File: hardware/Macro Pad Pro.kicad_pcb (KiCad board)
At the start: 2 copper layers, 107 x 134 mm, 149 parts, among them J1 USB_C, J2 Conn_02x08_Odd_Even, J4 Conn_02x01, SW1 SW_Push_B, SW2 SW_Push_R, U1 RP2040, U2 OLED, U3 AP2112K-3.3, U4 USBLC6-2SC6, U6 W25Q128JVS, Y1 ABM8-272-T3

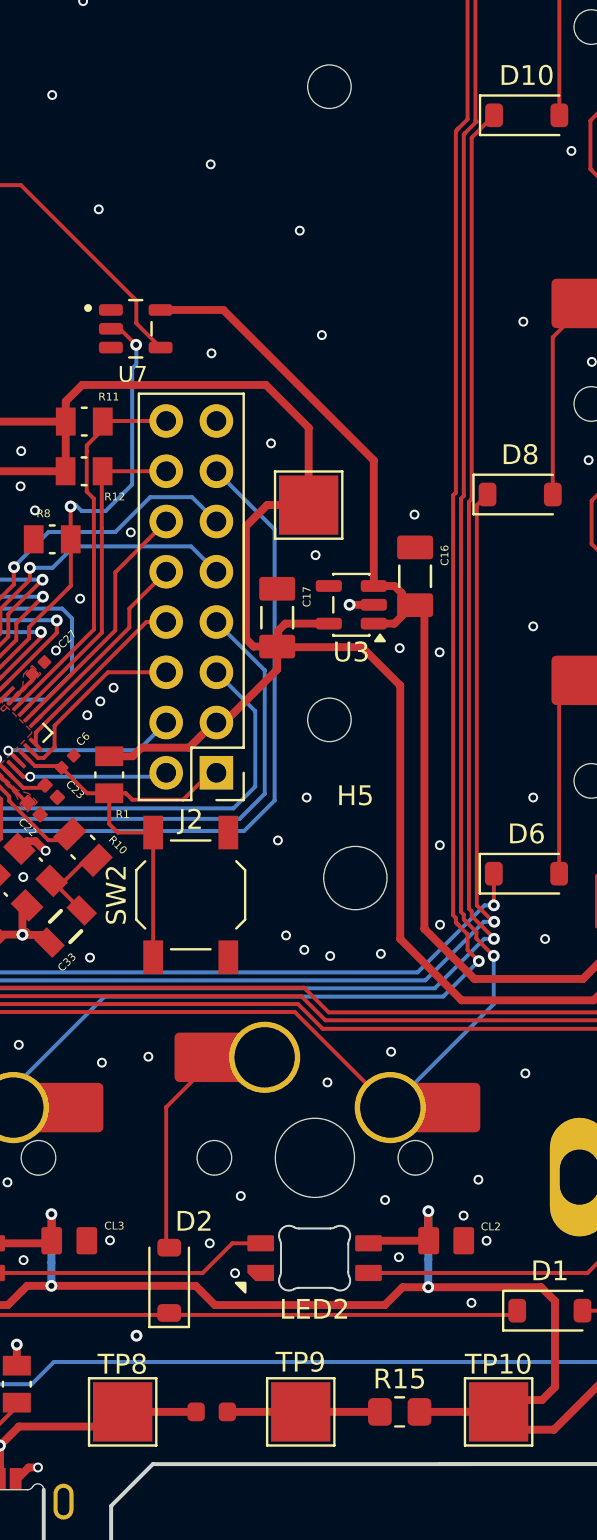
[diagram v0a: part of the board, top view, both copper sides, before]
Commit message: Update PCB design; add production and prototype files
- Update KiCad PCB and schematic (ERC/footprint fixes)
- Regenerate v1.0.0 production package (BOM, positions, designators, netlist)
- Add JLCPCB and new PCBWay production outputs
- Add 10uF 0805 footprint to Personal.pretty and brother.step
- Add prototype design/build photos
- Refresh design backups; remove stale lock files and old PCBWay run

Co-Authored-By: Claude Opus 4.8 <noreply@anthropic.com>
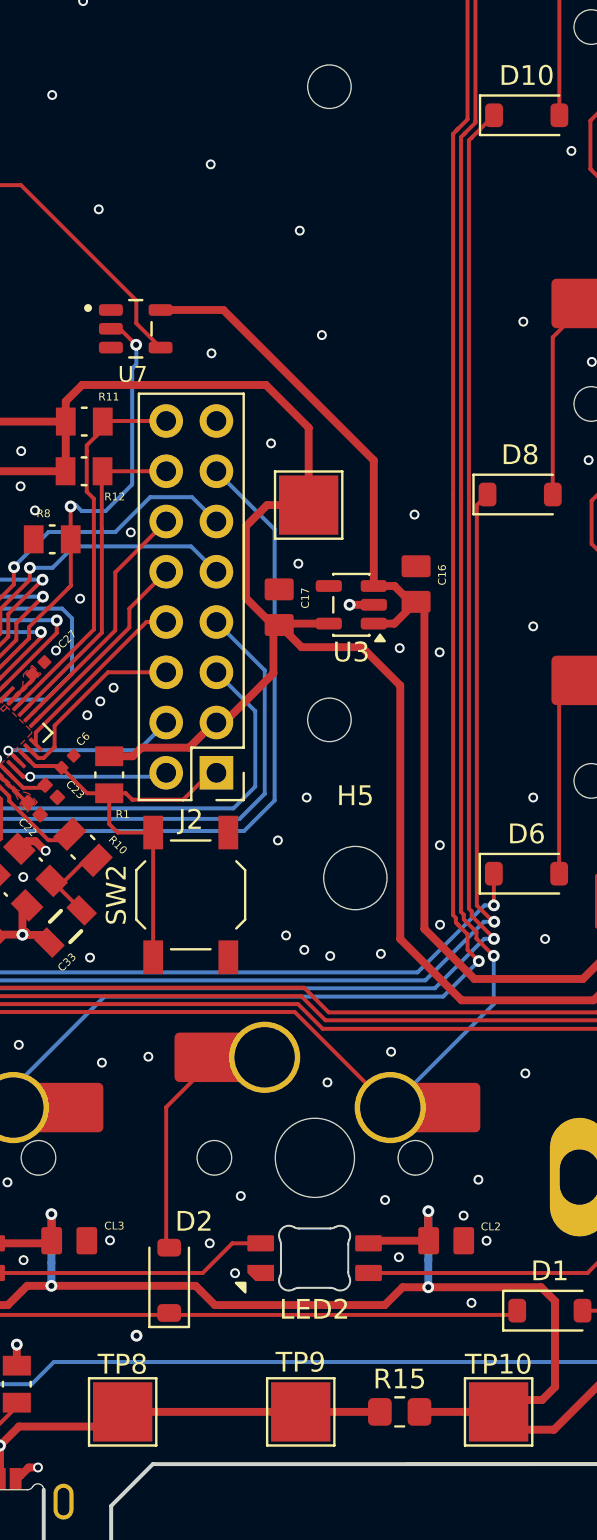
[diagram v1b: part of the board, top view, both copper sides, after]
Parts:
- removed F2: 1A, ScottoKeebs_Components:Fuse_0603
- C16, C17: footprint Personal:10uF_0805_CAPC3216X180N -> Personal:10uf_0805_CAPC2012X145N
- moved C17 0.54 mm to (112.3, 131.1)
- moved C16 0.39 mm to (119.2, 130.0)
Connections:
- R15 pad 1: Net-(F2-Pad2) -> VBUS
- TP9 pad 1: Net-(F2-Pad2) -> VBUS
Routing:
- net VBUS: track 27.2 -> 36.5 mm
- net Net-(F2-Pad2): track 7.71 -> 0.00 mm
- net +5V: track 751.8 -> 752.9 mm
- net +3.3V: track 183.3 -> 182.4 mm
